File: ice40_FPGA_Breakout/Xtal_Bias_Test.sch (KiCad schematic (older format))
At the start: 0 parts

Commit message: Add SPI EEPROM logic for SPI switching
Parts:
- added C? (x2): 15pf, symbol C
- added C? (x2): 0.01uf, symbol C
- added C? (x2): 0.1uf, symbol C
- added D? (x7): LED, symbol LED
- added J? (x5): 4POS_JUMPER, symbol 4POS_JUMPER
- added R? (x2): 10K, symbol R
- added R? (x7): 330, symbol R
- added X?: OSC_6-SMD, symbol OSC_6-SMD
- added X?: OSC_4-SMD, symbol OSC_4-SMD
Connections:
- new net: D?.2 (A), R?.2 (x7)
- new net 3V3_EXT_IN: C?.1, C?.1, C?.1, C?.1, R?.1, R?.1, R?.1, R?.1, R?.1, R?.1, R?.1, R?.1, R?.1, X?.4 (VDD), X?.6 (VDD)
- new net CMOS_CLK1: C?.1, X?.4 (CLK)
- new net CMOS_CLK2: C?.1, X?.3 (GND)
- new net CRYSTAL1_EN: R?.2, X?.1 (EN)
- new net CRYSTAL2_EN: R?.2, X?.1 (EN)
- new net EXT_SPI_MISO: J?.3 (P3)
- new net EXT_SPI_MOSI: J?.3 (P3)
- new net EXT_SPI_SCK: J?.3 (P3)
- new net EXT_SPI_SS: J?.3 (P3)
- new net FTDI_AD0_SCK: J?.1 (P1)
- new net FTDI_AD1_MOSI: J?.1 (P1)
- new net FTDI_AD2_MISO: J?.1 (P1)
- new net FTDI_AD3_SS: J?.1 (P1)
- new net GND: C?.2, C?.2, C?.2, C?.2, C?.2, C?.2, X?.3 (GND), X?.3 (GND)
- new net LED1: D?.1 (K)
- new net LED2: D?.1 (K)
- new net LED3: D?.1 (K)
- new net LED4: D?.1 (K)
- new net LED5: D?.1 (K)
- new net LED6: D?.1 (K)
- new net LED7: D?.1 (K)
- new net iCE_SPI_DATA1: J?.2 (P2), J?.4 (P4)
- new net iCE_SPI_DATA2: J?.3 (P3), J?.4 (P4)
- new net iCE_SPI_SCK: J?.4 (P4)
- new net iCE_SPI_SDI: J?.4 (P4)
- new net iCE_SPI_SDO: J?.1 (P1)
- new net iCE_SPI_SS: J?.4 (P4)
- new net s_FLASH_MISO: J?.2 (P2)
- new net s_FLASH_MOSI: J?.2 (P2)
- new net s_FLASH_SCK: J?.2 (P2), J?.2 (P2)
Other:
- note added: "Config 1 "="\nFTDI SPI --->FLASH SPI\nEXT SPI ---> iCE SPI\n\nConfig 2 "||"\nFTDI SPI ---> EXT SPI\nFLASH SPI ---> iCE SPI"
- note added: "Switch iCE Master to Slave\n"

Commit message: global nets changed to hierarchy net, interconnects updated
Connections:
- net s_FLASH_SCK: no longer J?.2 (P2)
- net 3V3_EXT_IN renamed 3V3_IN
- net CRYSTAL1_EN renamed XTAL1_EN
- net CRYSTAL2_EN renamed XTAL2_EN
- new net s_FLASH_SS: J?.2 (P2)
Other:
- note added: "LED 1-7 PULL DOWN"
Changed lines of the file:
@@
 $Descr A4 11693 8268
 encoding utf-8
-Sheet 7 7
+Sheet 6 7
 Title ""
 Date ""
@@
 	1    0    0    -1
 $EndComp
-Text GLabel 1950 2250 0    39   Input ~ 0
-3V3_EXT_IN
-$Comp
-L GND #PWR?
+$Comp
+L GND #PWR033
 U 1 1 5A30306B
 P 2300 3100
-F 0 "#PWR?" H 2300 2850 50  0001 C CNN
+F 0 "#PWR033" H 2300 2850 50  0001 C CNN
 F 1 "GND" H 2450 3050 50  0000 C CNN
 F 2 "" H 2300 3100 50  0001 C CNN
@@
 $EndComp
 $Comp
-L GND #PWR?
+L GND #PWR034
 U 1 1 5A303071
 P 3150 3050
-F 0 "#PWR?" H 3150 2800 50  0001 C CNN
+F 0 "#PWR034" H 3150 2800 50  0001 C CNN
 F 1 "GND" H 3300 3000 50  0000 C CNN
 F 2 "" H 3150 3050 50  0001 C CNN
@@
 	1    0    0    -1
 $EndComp
-Text GLabel 3600 2250 2    39   Input ~ 0
-CMOS_CLK1
 Wire Wire Line
 	2600 2250 2600 2450
@@
 	2600 2850 1950 2850
 Connection ~ 2600 2850
-Text GLabel 1950 2850 0    39   Input ~ 0
-CRYSTAL1_EN
 $Comp
 L R R?
@@
 	1    0    0    -1
 $EndComp
-Text GLabel 1950 1100 0    39   Input ~ 0
-3V3_EXT_IN
-$Comp
-L GND #PWR?
+$Comp
+L GND #PWR035
 U 1 1 5A3030AF
 P 2300 1950
-F 0 "#PWR?" H 2300 1700 50  0001 C CNN
+F 0 "#PWR035" H 2300 1700 50  0001 C CNN
 F 1 "GND" H 2450 1900 50  0000 C CNN
 F 2 "" H 2300 1950 50  0001 C CNN
@@
 $EndComp
 $Comp
-L GND #PWR?
+L GND #PWR036
 U 1 1 5A3030B5
 P 3150 1900
-F 0 "#PWR?" H 3150 1650 50  0001 C CNN
+F 0 "#PWR036" H 3150 1650 50  0001 C CNN
 F 1 "GND" H 3300 1850 50  0000 C CNN
 F 2 "" H 3150 1900 50  0001 C CNN
@@
 	1    0    0    -1
 $EndComp
-Text GLabel 3600 1100 2    39   Input ~ 0
-CMOS_CLK2
 Wire Wire Line
 	2600 1100 2600 1300
 Wire Wire Line
-	1950 1100 2850 1100
+	1800 1100 2850 1100
 Wire Wire Line
 	2850 1100 2850 1150
@@
 	2600 1700 1950 1700
 Connection ~ 2600 1700
-Text GLabel 1950 1700 0    39   Input ~ 0
-CRYSTAL2_EN
 $Comp
 L OSC_4-SMD X?
@@
 	1    0    0    -1
 $EndComp
-Text GLabel 3350 3950 2    39   Input ~ 0
-3V3_EXT_IN
 Wire Wire Line
 	2650 4250 2900 4250
@@
 Wire Wire Line
 	2350 5450 2150 5450
-Text GLabel 2150 4250 0    39   Input ~ 0
-LED1
-Text GLabel 2150 4450 0    39   Input ~ 0
-LED2
-Text GLabel 2150 4650 0    39   Input ~ 0
-LED3
-Text GLabel 2150 4850 0    39   Input ~ 0
-LED4
-Text GLabel 2150 5050 0    39   Input ~ 0
-LED5
-Text GLabel 2150 5250 0    39   Input ~ 0
-LED6
-Text GLabel 2150 5450 0    39   Input ~ 0
-LED7
-Text GLabel 7900 2650 0    39   Input ~ 0
-FTDI_AD3_SS
-Text GLabel 7900 2250 0    39   Input ~ 0
-FTDI_AD0_SCK
-Text GLabel 7900 1850 0    39   Input ~ 0
-FTDI_AD1_MOSI
-Text GLabel 7900 1500 0    39   Input ~ 0
-FTDI_AD2_MISO
-Text GLabel 7900 1950 0    39   Input ~ 0
-EXT_SPI_MOSI
-Text GLabel 7900 1600 0    39   Input ~ 0
-EXT_SPI_MISO
-Text GLabel 7900 2350 0    39   Input ~ 0
-EXT_SPI_SCK
-Text GLabel 7900 2750 0    39   Input ~ 0
-EXT_SPI_SS
 $Comp
 L 4POS_JUMPER J?
@@
 	1    0    0    -1
 $EndComp
-Text GLabel 8700 1500 2    39   Input ~ 0
-s_FLASH_MOSI
-Text GLabel 8700 1850 2    39   Input ~ 0
-s_FLASH_MISO
-Text GLabel 8700 2350 2    39   Input ~ 0
-iCE_SPI_SCK
-Text GLabel 8700 2750 2    39   Input ~ 0
-iCE_SPI_SS
-Text GLabel 8700 2250 2    39   Input ~ 0
-s_FLASH_SCK
-Text GLabel 8700 2650 2    39   Input ~ 0
-s_FLASH_SCK
 Wire Wire Line
 	7900 2650 8050 2650
@@
 Wire Wire Line
 	8550 2650 8700 2650
-Text GLabel 8700 1600 2    39   Input ~ 0
-iCE_SPI_DATA1
-Text GLabel 8700 1950 2    39   Input ~ 0
-iCE_SPI_DATA2
 Wire Wire Line
 	7900 1600 8050 1600
@@
 Wire Wire Line
 	8050 3250 7900 3250
-Text GLabel 7900 3150 0    39   Input ~ 0
-iCE_SPI_SDO
-Text GLabel 7900 3250 0    39   Input ~ 0
-iCE_SPI_DATA2
-Text GLabel 8700 3150 2    39   Input ~ 0
-iCE_SPI_DATA1
-Text GLabel 8700 3250 2    39   Input ~ 0
-iCE_SPI_SDI
 Text Notes 8950 2950 2    60   ~ 0
 Switch iCE Master to Slave\n
 Text Notes 7750 1300 0    60   ~ 0
 Config 1 "="\nFTDI SPI --->FLASH SPI\nEXT SPI ---> iCE SPI\n\nConfig 2 "||"\nFTDI SPI ---> EXT SPI\nFLASH SPI ---> iCE SPI
+Text HLabel 1800 1100 0    39   Input Italic 8
+3V3_IN
+Text HLabel 1950 1700 0    39   Input Italic 8
+XTAL2_EN
+Text HLabel 1950 2850 0    39   Input Italic 8
+XTAL1_EN
+Text HLabel 1950 2250 0    39   Input Italic 8
+3V3_IN
+Text HLabel 2150 4250 0    39   Input Italic 8
+LED1
+Text HLabel 2150 4450 0    39   Input Italic 8
+LED2
+Text HLabel 2150 4650 0    39   Input Italic 8
+LED3
+Text HLabel 2150 4850 0    39   Input Italic 8
+LED4
+Text HLabel 2150 5050 0    39   Input Italic 8
+LED5
+Text HLabel 2150 5250 0    39   Input Italic 8
+LED6
+Text HLabel 2150 5450 0    39   Input Italic 8
+LED7
+Text HLabel 7900 1500 0    39   Input Italic 8
+FTDI_AD2_MISO
+Text HLabel 7900 1600 0    39   Input Italic 8
+EXT_SPI_MISO
+Text HLabel 7900 1850 0    39   Input Italic 8
+FTDI_AD1_MOSI
+Text HLabel 7900 1950 0    39   Input Italic 8
+EXT_SPI_MOSI
+Text HLabel 7900 2250 0    39   Input Italic 8
+FTDI_AD0_SCK
+Text HLabel 7900 2350 0    39   Input Italic 8
+EXT_SPI_SCK
+Text HLabel 7900 2650 0    39   Input Italic 8
+FTDI_AD3_SS
+Text HLabel 7900 2750 0    39   Input Italic 8
+EXT_SPI_SS
+Text HLabel 7900 3150 0    39   Input Italic 8
+iCE_SPI_SDO
+Text HLabel 8700 1500 2    39   Input Italic 8
+s_FLASH_MOSI
+Text HLabel 8700 1850 2    39   Input Italic 8
+s_FLASH_MISO
+Text HLabel 8700 2250 2    39   Input Italic 8
+s_FLASH_SCK
+Text HLabel 8700 2350 2    39   Input Italic 8
+iCE_SPI_SCK
+Text HLabel 8700 2750 2    39   Input Italic 8
+iCE_SPI_SS
+Text HLabel 8700 3250 2    39   Input Italic 8
+iCE_SPI_SDI
+Text HLabel 3350 3950 2    39   Input Italic 8
+3V3_IN
+Text HLabel 3600 1100 2    39   Input Italic 8
+CMOS_CLK2
+Text HLabel 3600 2250 2    39   Input Italic 8
+CMOS_CLK1
+Text Notes 2950 3950 2    39   Italic 8
+LED 1-7 PULL DOWN
+Text HLabel 8700 2650 2    39   Input Italic 8
+s_FLASH_SS
+Text GLabel 8700 1600 2    39   Input Italic 8
+iCE_SPI_DATA1
+Text GLabel 8700 1950 2    39   Input Italic 8
+iCE_SPI_DATA2
+Text GLabel 8700 3150 2    39   Input Italic 8
+iCE_SPI_DATA1
+Text GLabel 7900 3250 0    39   Input Italic 8
+iCE_SPI_DATA2
+Text HLabel 1700 1200 0    39   Input Italic 8
+GND
+$Comp
+L GND #PWR037
+U 1 1 5A406131
+P 1800 1250
+F 0 "#PWR037" H 1800 1000 50  0001 C CNN
+F 1 "GND" H 1950 1200 50  0000 C CNN
+F 2 "" H 1800 1250 50  0001 C CNN
+F 3 "" H 1800 1250 50  0001 C CNN
+	1    1800 1250
+	1    0    0    -1
+$EndComp
+Wire Wire Line
+	1700 1200 1800 1200
+Wire Wire Line
+	1800 1200 1800 1250
 $EndSCHEMATC

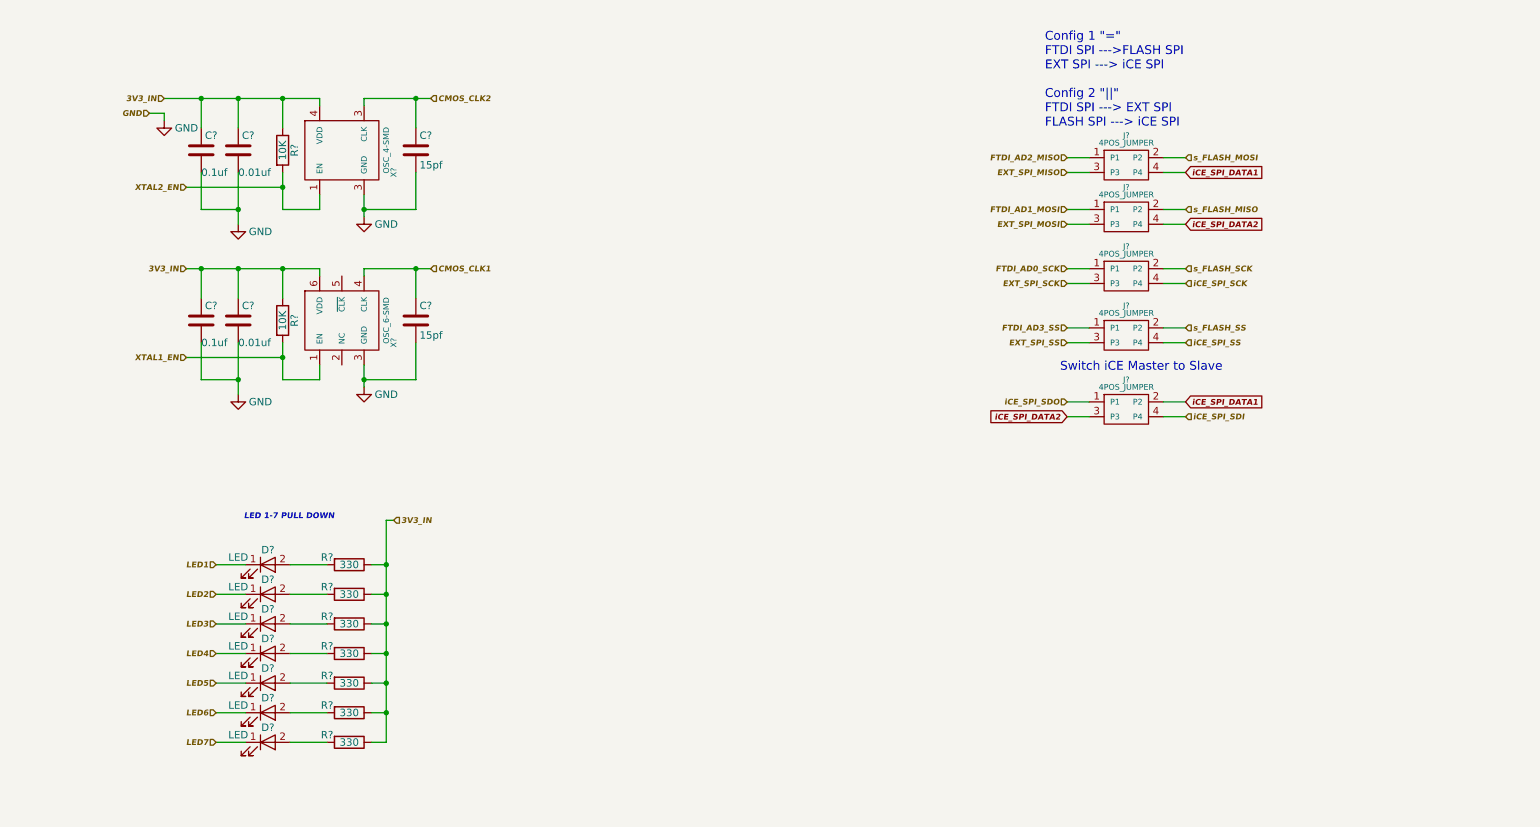
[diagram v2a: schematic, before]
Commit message: memory modules added
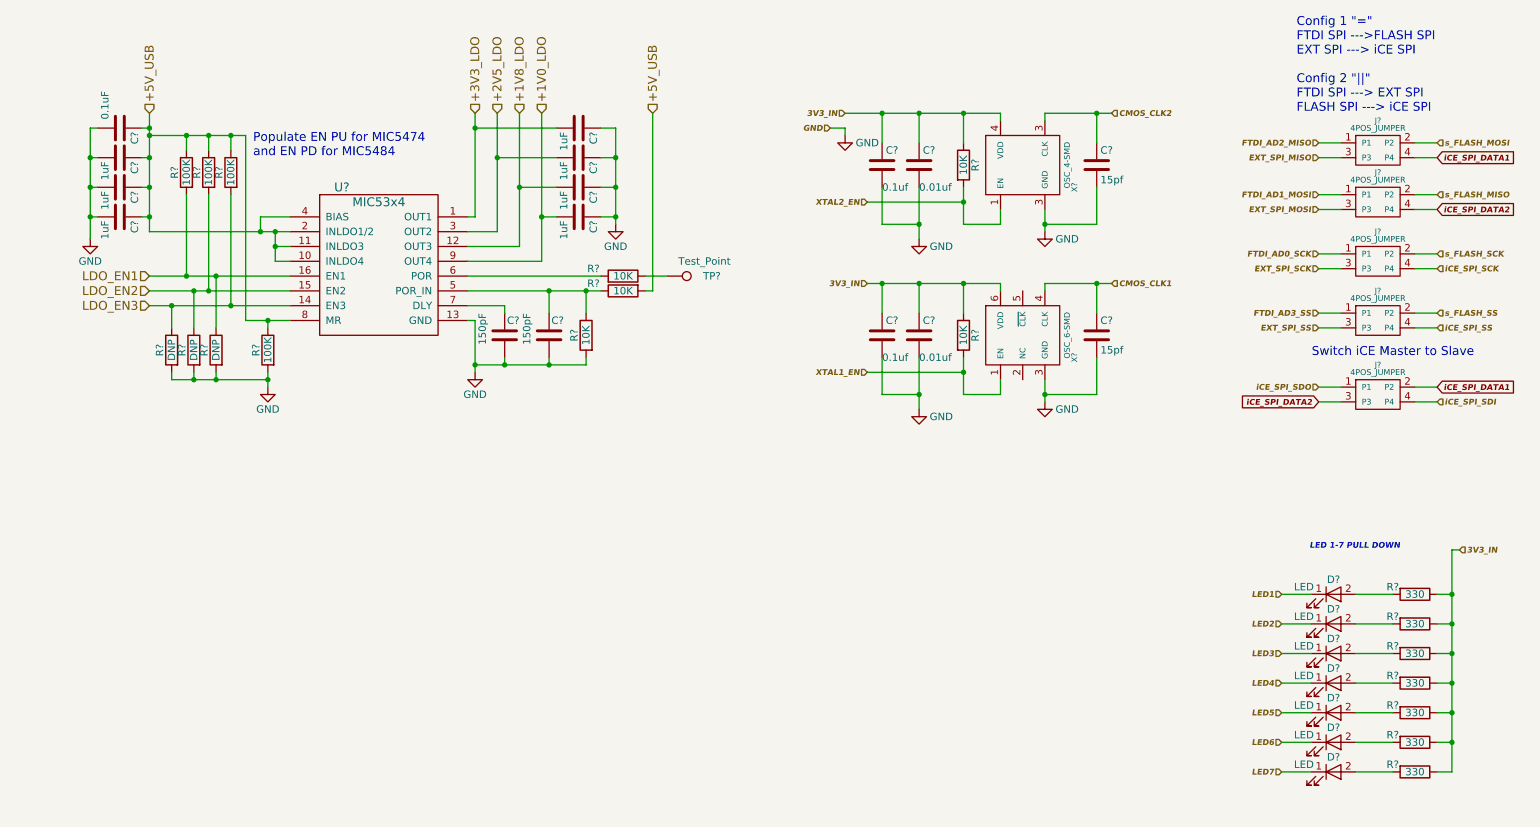
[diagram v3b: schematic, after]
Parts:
- added C? (x7): 1uF, symbol C
- added C?: 0.1uF, symbol C
- added C? (x2): 150pF, symbol C
- added R? (x4): 100K, symbol R
- added R? (x3): 10K, symbol R
- added R? (x3): DNP, symbol R
- added TP?: Test_Point, symbol Test_Point
- added U?: MIC53x4, symbol MIC53x4
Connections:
- net GND: now also C?.1, C?.1, C?.1, C?.1, C?.1, C?.1, C?.2, C?.2, C?.2, C?.2, R?.2, R?.2, R?.2, R?.2, R?.2, U?.13 (GND)
- new net: C?.2, R?.1, R?.1, U?.5 (POR_IN)
- new net: R?.2, U?.6 (POR)
- new net: C?.2, U?.7 (DLY)
- new net: R?.1, TP?.1
- new net +1V0_LDO: C?.2, U?.9 (OUT4)
- new net +1V8_LDO: C?.2, U?.12 (OUT3)
- new net +2V5_LDO: C?.2, U?.3 (OUT2)
- new net +3V3_LDO: C?.2, U?.1 (OUT1)
- new net +5V_USB: C?.1, C?.1, C?.1, C?.1, R?.1, R?.1, R?.1, R?.1, R?.2, U?.10 (INLDO4), U?.11 (INLDO3), U?.2 (INLDO1/2), U?.4 (BIAS), U?.8 (MR)
- new net LDO_EN1: R?.1, R?.2, U?.16 (EN1)
- new net LDO_EN2: R?.1, R?.2, U?.15 (EN2)
- new net LDO_EN3: R?.1, R?.2, U?.14 (EN3)
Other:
- note added: "Populate EN PU for MIC5474 \nand EN PD for MIC5484"
- moved on the sheet: C?, D?, J?, R?, X?

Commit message: post review fix
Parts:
- added D?: LED, symbol LED
- added R? (x8): 0, symbol R
- added R?: 330, symbol R
- R? (x3): value 100K -> 10K
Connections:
- net +1V0_LDO: now also R?.1; no longer C?.2, U?.9 (OUT4)
- net +1V8_LDO: now also R?.1; no longer C?.2, U?.12 (OUT3)
- net +2V5_LDO: now also R?.1; no longer C?.2, U?.3 (OUT2)
- net +3V3_LDO: now also R?.1; no longer C?.2, U?.1 (OUT1)
- net +5V_USB: now also R?.1; no longer C?.1, C?.1, C?.1, C?.1, R?.1, R?.1, R?.1, R?.1, U?.10 (INLDO4), U?.11 (INLDO3), U?.2 (INLDO1/2), U?.4 (BIAS), U?.8 (MR)
- net 3V3_IN: now also R?.1
- net LDO_EN1: now also R?.2; no longer R?.1, R?.2, U?.16 (EN1)
- net LDO_EN2: now also R?.2; no longer R?.1, R?.2, U?.15 (EN2)
- net LDO_EN3: now also R?.2; no longer R?.1, R?.2, U?.14 (EN3)
- new net: C?.2, R?.2, U?.1 (OUT1)
- new net: C?.1, C?.1, C?.1, C?.1, R?.1, R?.1, R?.1, R?.1, R?.2, U?.10 (INLDO4), U?.11 (INLDO3), U?.2 (INLDO1/2), U?.4 (BIAS), U?.8 (MR)
- new net: C?.2, R?.2, U?.12 (OUT3)
- new net: R?.1, R?.1, R?.2, U?.14 (EN3)
- new net: R?.1, R?.1, R?.2, U?.15 (EN2)
- new net: R?.1, R?.1, R?.2, U?.16 (EN1)
- new net: C?.2, R?.2, U?.3 (OUT2)
- new net: C?.2, R?.2, U?.9 (OUT4)
- new net: D?.2 (A), R?.2
- new net LED8: D?.1 (K)
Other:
- moved on the sheet: C?, R?, TP?, U?

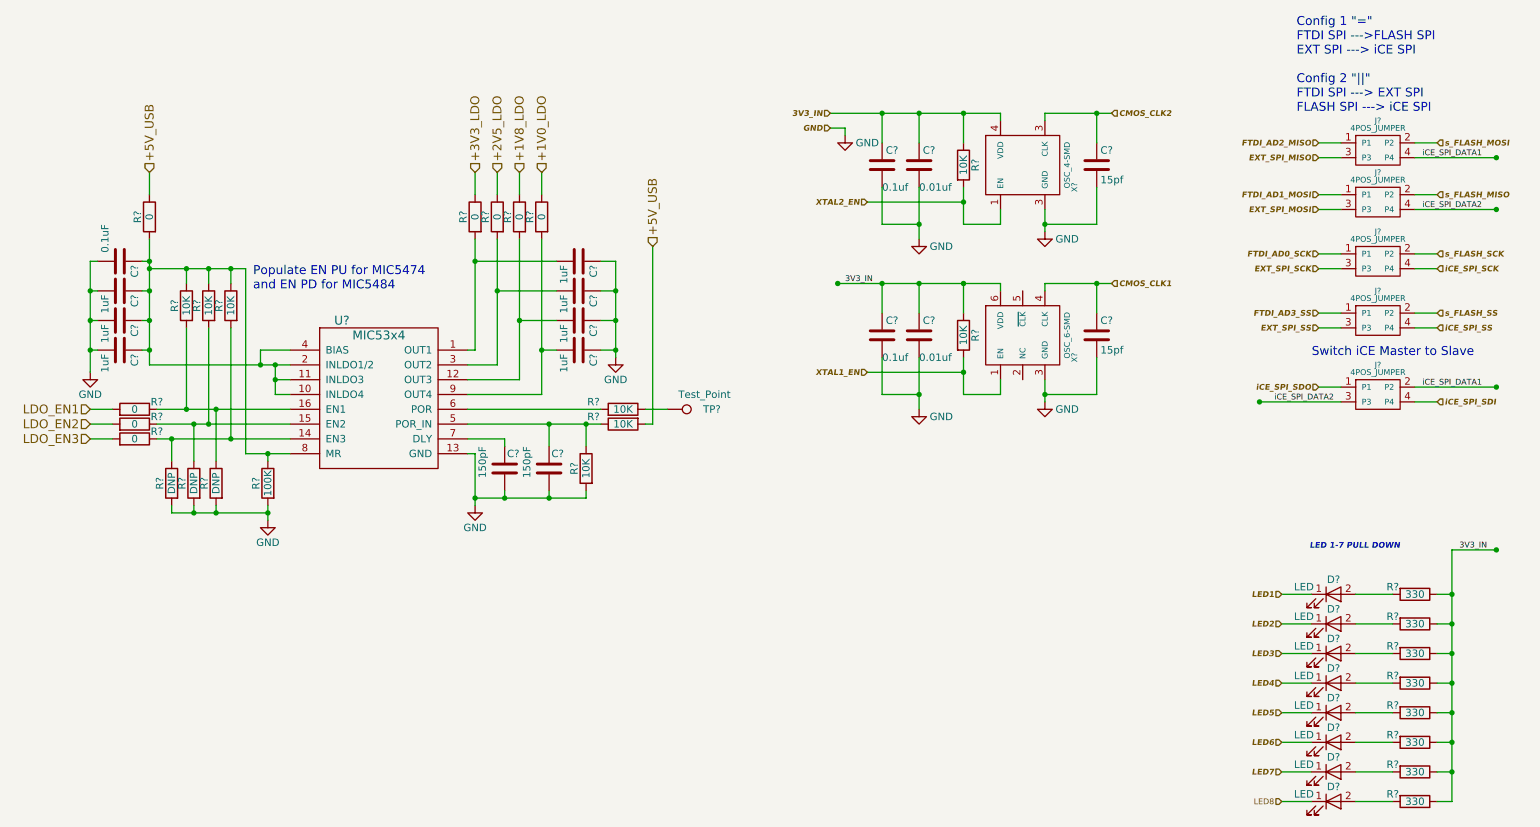
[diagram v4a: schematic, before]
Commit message: Component Annotated and R/C/Conn/TP CVPCB mapping
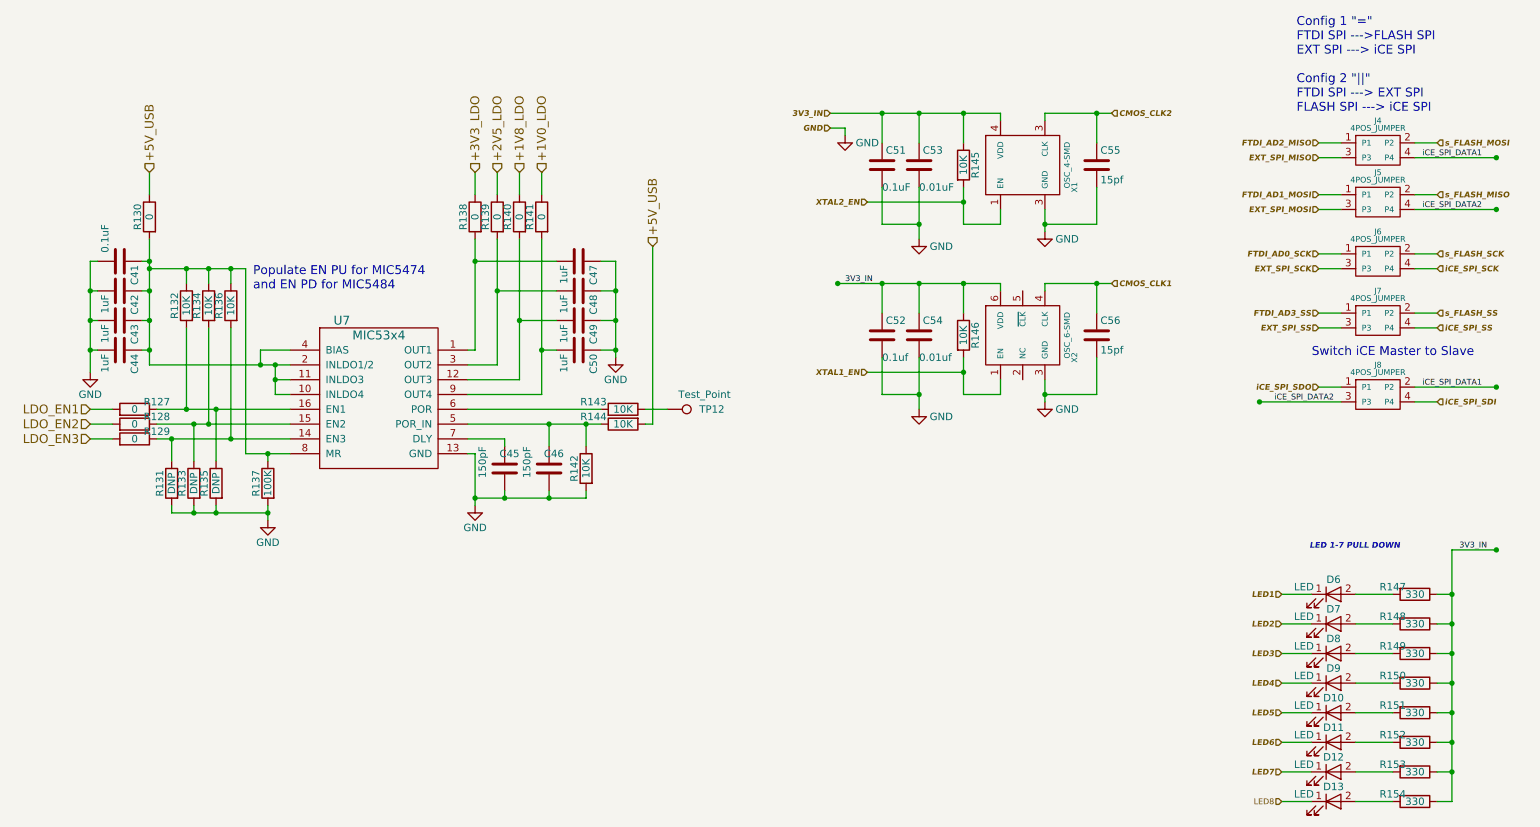
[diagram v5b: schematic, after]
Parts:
- C51: renamed from C?; value 0.1uf -> 0.1uF
- C53: renamed from C?; value 0.01uf -> 0.01uF
- gave numbers to parts that had none: 59
